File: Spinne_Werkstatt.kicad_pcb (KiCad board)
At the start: 2 copper layers, 42 x 82 mm, 17 parts, among them J1 Conn_01x02_Pin, J3 Conn_01x03_Pin, Q1 BSS138, Q2 BSS138, U1 ESP32-WROOM-32UE, U2 CH340C

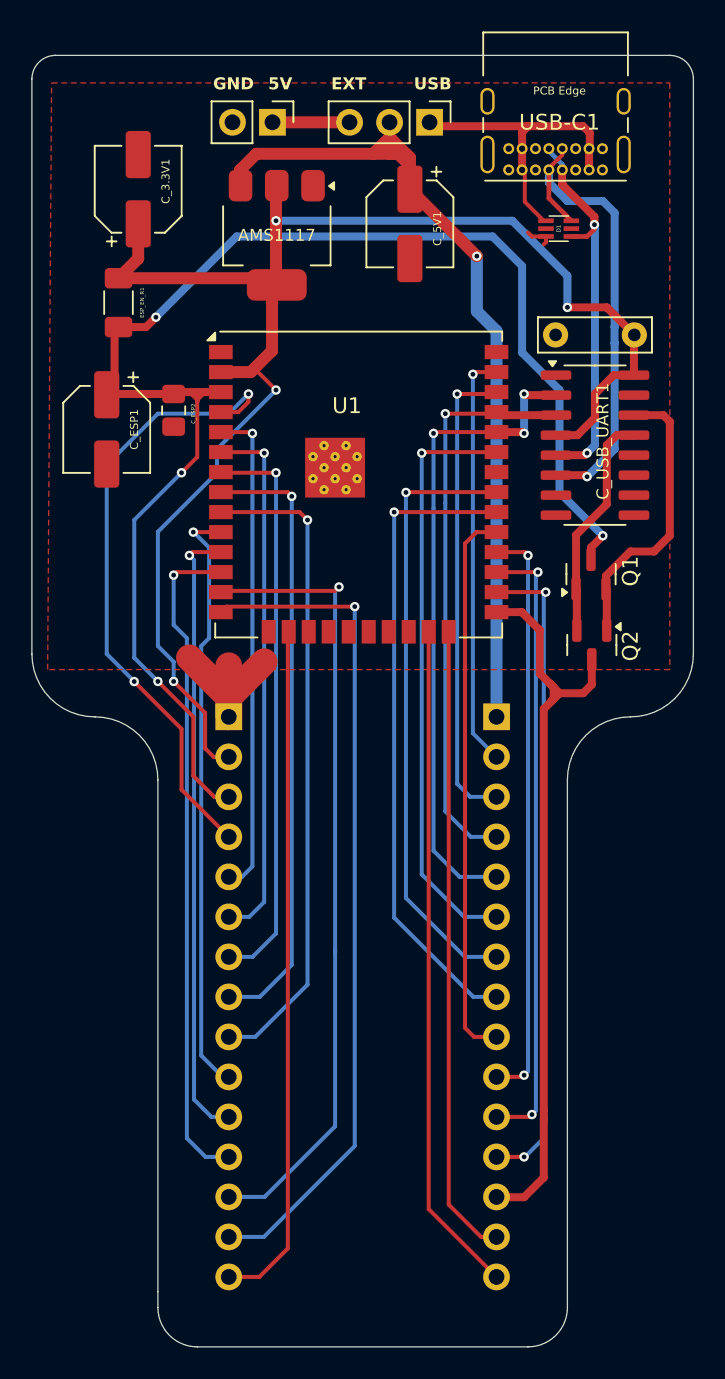
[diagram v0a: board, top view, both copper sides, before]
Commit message: improved ground plain -- version 1.1.2
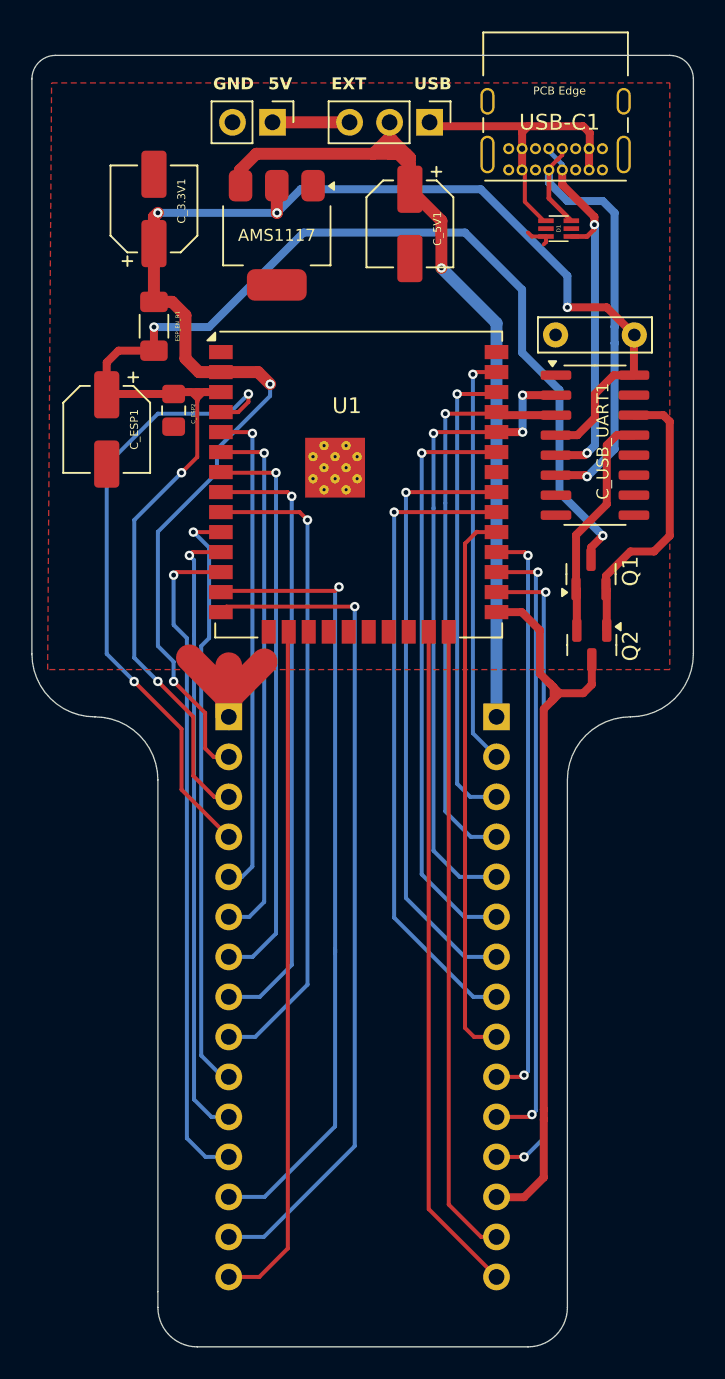
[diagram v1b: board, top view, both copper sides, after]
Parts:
- moved ESP_EN_R1 2.70 mm to (126.2, 52.7)
- moved C_3.3V1 1.60 mm to (126.2, 45.2)
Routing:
- net +3V3: track 96.1 -> 94.9 mm, vias 4 -> 5

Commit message: added IO Names, improved vias
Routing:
- net pin30: track 40.8 -> 43.2 mm
- net pin23: track 42.7 -> 44.2 mm
- net pin31: track 38.8 -> 40.2 mm
- net pin33: track 37.4 -> 38.8 mm
- net pin37: track 26.5 -> 27.8 mm
- net ESP_TX: track 36.3 -> 37.4 mm
- net ESP_RX: track 41.2 -> 42.2 mm
- net pin9: track 41.6 -> 42.6 mm
- net pin5: track 31.3 -> 32.2 mm
- net pin7: track 36.4 -> 37.1 mm
- net pin36: track 30.1 -> 30.9 mm
- net pin13: track 51.1 -> 50.4 mm
- net pin6: track 33.9 -> 34.6 mm
- net pin8: track 39.2 -> 39.8 mm
- net ESP32_EN: track 94.2 -> 93.5 mm
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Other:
- board text added: "3.3V"
- board text added: "EN"
- board text added: "GPIO12"
- board text added: "GPIO13"
- board text added: "GPIO14"
- board text added: "GPIO25"
- board text added: "GPIO26"
- board text added: "GPIO27"
- board text added: "GPIO32"
- board text added: "GPIO33"
- board text added: "GPIO34"
- board text added: "GPIO35"
- board text added: "VN"
- board text added: "VP"

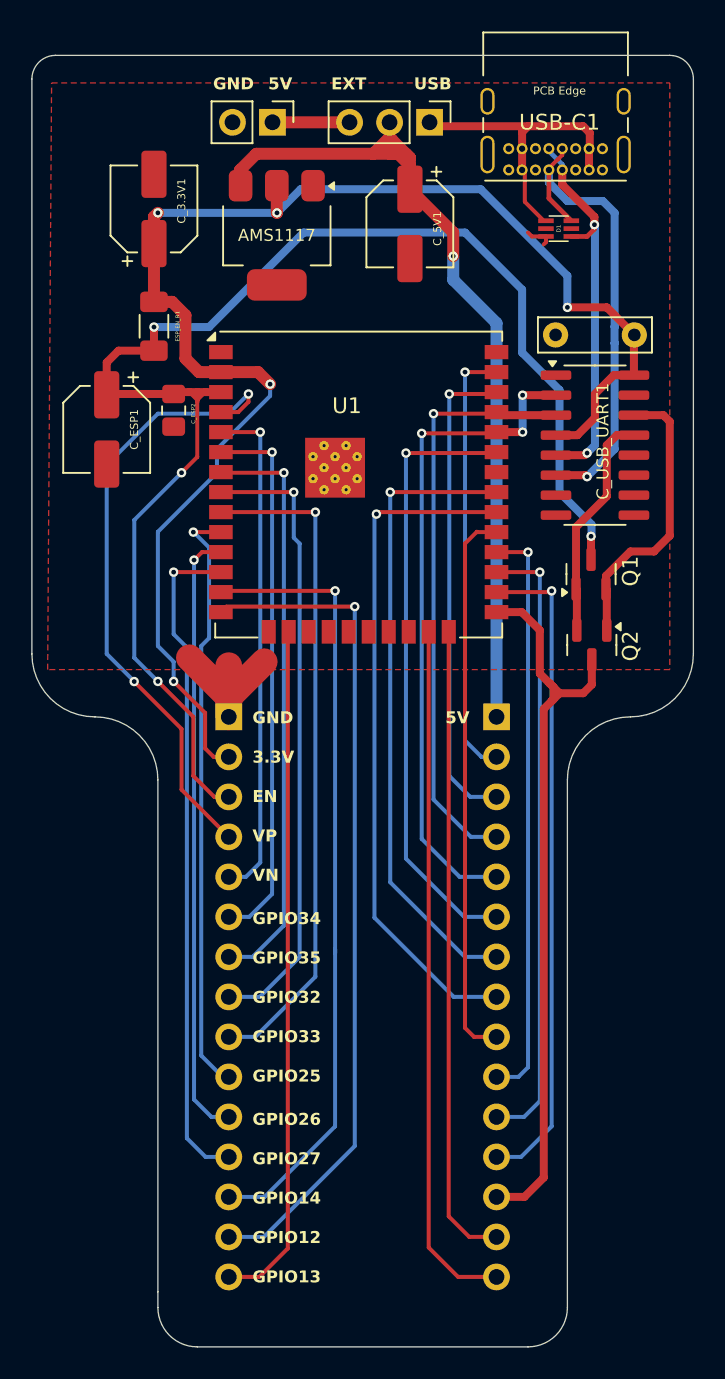
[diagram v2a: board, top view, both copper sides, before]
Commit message: improved clearences around uart capacitor
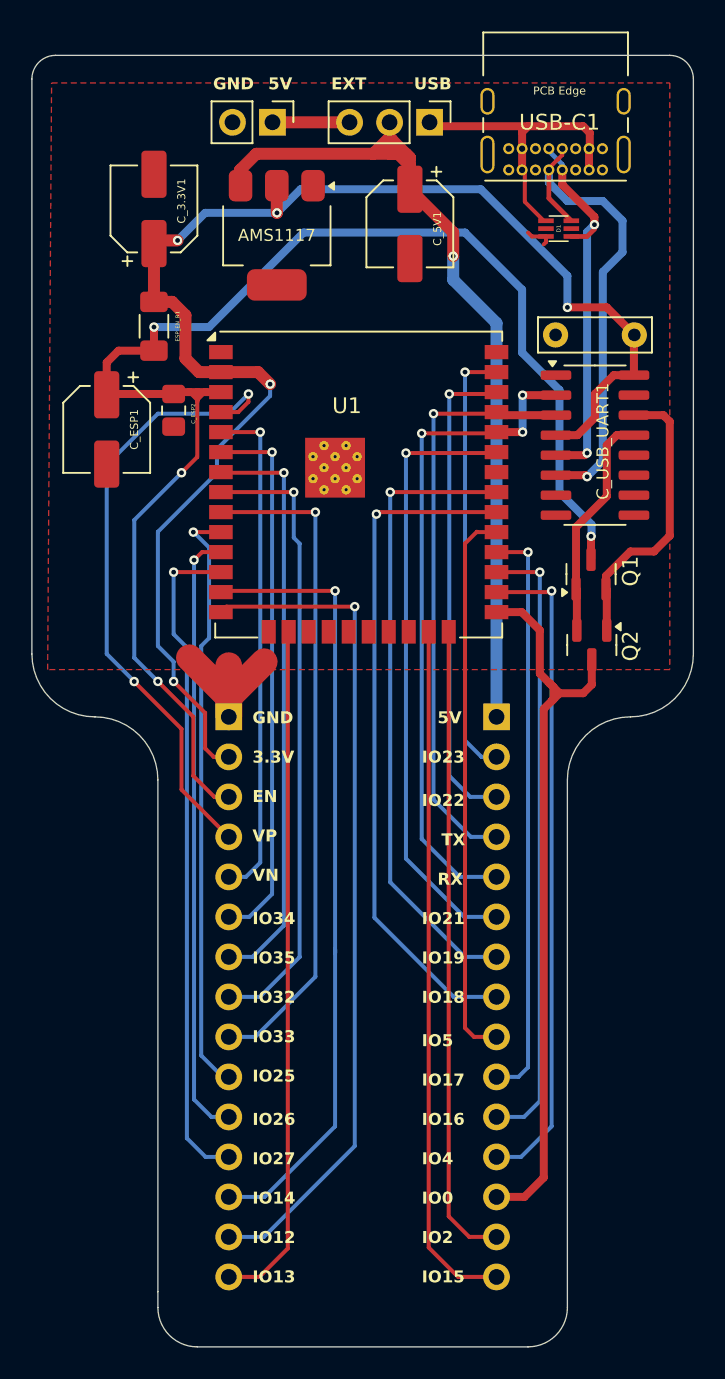
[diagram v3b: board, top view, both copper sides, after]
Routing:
- net +3V3: track 94.9 -> 93.9 mm
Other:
- board text added: "IO0"
- board text added: "IO12"
- board text added: "IO13"
- board text added: "IO14"
- board text added: "IO15"
- board text added: "IO16"
- board text added: "IO17"
- board text added: "IO18"
- board text added: "IO19"
- board text added: "IO2"
- board text added: "IO21"
- board text added: "IO22"
- board text added: "IO23"
- board text added: "IO25"
- board text added: "IO26"
- board text added: "IO27"
- board text added: "IO32"
- board text added: "IO33"
- board text added: "IO34"
- board text added: "IO35"
- board text added: "IO4"
- board text added: "IO5"
- board text added: "RX"
- board text added: "TX"
- board text removed: "GPIO12"
- board text removed: "GPIO13"
- board text removed: "GPIO14"
- board text removed: "GPIO25"
- board text removed: "GPIO26"
- board text removed: "GPIO27"
- board text removed: "GPIO32"
- board text removed: "GPIO33"
- board text removed: "GPIO34"
- board text removed: "GPIO35"
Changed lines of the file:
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@@
 		(layer "Edge.Cuts")
+	)
+	(gr_text "IO22"
+		(at 143.25 83.25 0)
+		(layer "F.SilkS")
+		(effects
+			(font
+				(size 0.762 0.762)
+				(thickness 0.1905)
+				(bold yes)
+			)
+			(justify left bottom)
+		)
 	)
 	(gr_text "USB"
@@
 	)
 	(gr_text "5V\n"
-		(at 144.75 78 0)
+		(at 144.25 78 0)
 		(layer "F.SilkS")
 		(effects
@@
 		)
 	)
-	(gr_text "GPIO25"
+	(gr_text "IO5"
+		(at 143.25 98.5 0)
+		(layer "F.SilkS")
+		(effects
+			(font
+				(size 0.762 0.762)
+				(thickness 0.1905)
+				(bold yes)
+			)
+			(justify left bottom)
+		)
+	)
+	(gr_text "IO25"
 		(at 132.5 100.75 0)
 		(layer "F.SilkS")
@@
 		)
 	)
-	(gr_text "GPIO26"
+	(gr_text "IO26"
 		(at 132.5 103.5 0)
 		(layer "F.SilkS")
@@
 		)
 	)
-	(gr_text "GPIO34"
+	(gr_text "IO34"
 		(at 132.5 90.75 0)
+		(layer "F.SilkS")
+		(effects
+			(font
+				(size 0.762 0.762)
+				(thickness 0.1905)
+				(bold yes)
+			)
+			(justify left bottom)
+		)
+	)
+	(gr_text "IO4"
+		(at 143.25 106 0)
 		(layer "F.SilkS")
 		(effects
@@
 		)
 	)
-	(gr_text "GPIO27\n"
+	(gr_text "TX\n"
+		(at 144.5 85.75 0)
+		(layer "F.SilkS")
+		(effects
+			(font
+				(size 0.762 0.762)
+				(thickness 0.1905)
+				(bold yes)
+			)
+			(justify left bottom)
+		)
+	)
+	(gr_text "IO23"
+		(at 143.25 80.5 0)
+		(layer "F.SilkS")
+		(effects
+			(font
+				(size 0.762 0.762)
+				(thickness 0.1905)
+				(bold yes)
+			)
+			(justify left bottom)
+		)
+	)
+	(gr_text "IO0"
+		(at 143.25 108.5 0)
+		(layer "F.SilkS")
+		(effects
+			(font
+				(size 0.762 0.762)
+				(thickness 0.1905)
+				(bold yes)
+			)
+			(justify left bottom)
+		)
+	)
+	(gr_text "IO2"
+		(at 143.25 111 0)
+		(layer "F.SilkS")
+		(effects
+			(font
+				(size 0.762 0.762)
+				(thickness 0.1905)
+				(bold yes)
+			)
+			(justify left bottom)
+		)
+	)
+	(gr_text "IO27\n"
 		(at 132.5 106 0)
 		(layer "F.SilkS")
@@
 		)
 	)
-	(gr_text "GPIO14"
+	(gr_text "IO15"
+		(at 143.25 113.5 0)
+		(layer "F.SilkS")
+		(effects
+			(font
+				(size 0.762 0.762)
+				(thickness 0.1905)
+				(bold yes)
+			)
+			(justify left bottom)
+		)
+	)
+	(gr_text "IO16"
+		(at 143.25 103.5 0)
+		(layer "F.SilkS")
+		(effects
+			(font
+				(size 0.762 0.762)
+				(thickness 0.1905)
+				(bold yes)
+			)
+			(justify left bottom)
+		)
+	)
+	(gr_text "IO21"
+		(at 143.25 90.75 0)
+		(layer "F.SilkS")
+		(effects
+			(font
+				(size 0.762 0.762)
+				(thickness 0.1905)
+				(bold yes)
+			)
+			(justify left bottom)
+		)
+	)
+	(gr_text "IO14"
 		(at 132.5 108.5 0)
 		(layer "F.SilkS")
@@
 		)
 	)
-	(gr_text "GPIO33"
+	(gr_text "IO18"
+		(at 143.25 95.75 0)
+		(layer "F.SilkS")
+		(effects
+			(font
+				(size 0.762 0.762)
+				(thickness 0.1905)
+				(bold yes)
+			)
+			(justify left bottom)
+		)
+	)
+	(gr_text "IO33"
 		(at 132.5 98.25 0)
 		(layer "F.SilkS")
@@
 		)
 	)
-	(gr_text "GPIO12"
+	(gr_text "IO12"
 		(at 132.5 111 0)
 		(layer "F.SilkS")
@@
 		)
 	)
-	(gr_text "GPIO13"
+	(gr_text "IO13"
 		(at 132.5 113.5 0)
 		(layer "F.SilkS")
@@
 		)
 	)
-	(gr_text "GPIO32"
+	(gr_text "RX"
+		(at 144.25 88.25 0)
+		(layer "F.SilkS")
+		(effects
+			(font
+				(size 0.762 0.762)
+				(thickness 0.1905)
+				(bold yes)
+			)
+			(justify left bottom)
+		)
+	)
+	(gr_text "IO32"
 		(at 132.5 95.75 0)
 		(layer "F.SilkS")
@@
 		)
 	)
-	(gr_text "GPIO35\n"
+	(gr_text "IO19"
+		(at 143.25 93.25 0)
+		(layer "F.SilkS")
+		(effects
+			(font
+				(size 0.762 0.762)
+				(thickness 0.1905)
+				(bold yes)
+			)
+			(justify left bottom)
+		)
+	)
+	(gr_text "IO17"
+		(at 143.25 101 0)
+		(layer "F.SilkS")
+		(effects
+			(font
+				(size 0.762 0.762)
+				(thickness 0.1905)
+				(bold yes)
+			)
+			(justify left bottom)
+		)
+	)
+	(gr_text "IO35\n"
 		(at 132.5 93.25 0)
 		(layer "F.SilkS")
@@
 	)
 	(segment
+		(start 126.45 47.25)
+		(end 126.25 47.45)
+		(width 0.762)
+		(layer "F.Cu")
+		(net 3)
+	)
+	(segment
 		(start 127.4 51.15)
 		(end 128.25 52)
@@
 	)
 	(segment
+		(start 127.75 47.25)
+		(end 126.45 47.25)
+		(width 0.762)
+		(layer "F.Cu")
+		(net 3)
+	)
+	(segment
 		(start 134.05 45.4888)
 		(end 134.0612 45.5)
@@
 	)
 	(segment
-		(start 126.5 45.5)
-		(end 126.25 45.75)
-		(width 0.762)
-		(layer "F.Cu")
-		(net 3)
-	)
-	(segment
 		(start 126.25 51.15)
 		(end 127.4 51.15)
@@
 	)
 	(segment
-		(start 126.25 45.75)
-		(end 126.25 47.45)
-		(width 0.762)
-		(layer "F.Cu")
-		(net 3)
-	)
-	(segment
 		(start 128.25 54.75)
 		(end 129.11 55.61)
@@
 	)
 	(via
-		(at 126.5 45.5)
+		(at 127.75 47.25)
 		(size 0.6)
 		(drill 0.3)
@@
 	)
 	(segment
+		(start 129.5 45.5)
+		(end 127.75 47.25)
+		(width 0.508)
+		(layer "B.Cu")
+		(net 3)
+	)
+	(segment
 		(start 152.5 49.5)
 		(end 152.5 51.5)
@@
 	(segment
 		(start 134.0612 45.5)
-		(end 126.5 45.5)
+		(end 129.5 45.5)
 		(width 0.508)
 		(layer "B.Cu")
@@
 	)
 	(segment
-		(start 154.25 46.283159)
-		(end 154.25 60.25)
+		(start 153.75 46.716841)
+		(end 153.75 60.75)
 		(width 0.508)
 		(layer "B.Cu")
@@
 	(segment
 		(start 154.216841 46.25)
-		(end 154.25 46.283159)
-		(width 0.508)
-		(layer "B.Cu")
-		(net 35)
-	)
-	(segment
-		(start 154.25 60.25)
-		(end 153.75 60.75)
+		(end 153.75 46.716841)
 		(width 0.508)
 		(layer "B.Cu")
@@
 	)
 	(segment
+		(start 156 48)
+		(end 156 46)
+		(width 0.508)
+		(layer "B.Cu")
+		(net 36)
+	)
+	(segment
+		(start 154.75 61.25)
+		(end 154.75 49.25)
+		(width 0.508)
+		(layer "B.Cu")
+		(net 36)
+	)
+	(segment
 		(start 152.5 44.75)
+		(end 151.325 43.575)
+		(width 0.508)
+		(layer "B.Cu")
+		(net 36)
+	)
+	(segment
+		(start 151.325 43.575)
+		(end 151.325 42.775)
+		(width 0.508)
+		(layer "B.Cu")
+		(net 36)
+	)
+	(segment
+		(start 154.75 44.75)
+		(end 152.5 44.75)
+		(width 0.508)
+		(layer "B.Cu")
+		(net 36)
+	)
+	(segment
+		(start 153.75 62.25)
+		(end 154.75 61.25)
+		(width 0.508)
+		(layer "B.Cu")
+		(net 36)
+	)
+	(segment
+		(start 154.75 49.25)
+		(end 156 48)
+		(width 0.508)
+		(layer "B.Cu")
+		(net 36)
+	)
+	(segment
+		(start 156 46)
 		(end 154.75 44.75)
 		(width 0.508)
 		(layer "B.Cu")
-		(net 36)
-	)
-	(segment
-		(start 155.495 53.769839)
-		(end 155.5 53.774839)
-		(width 0.508)
-		(layer "B.Cu")
-		(net 36)
-	)
-	(segment
-		(start 155.5 52.725161)
-		(end 155.495 52.730161)
-		(width 0.508)
-		(layer "B.Cu")
-		(net 36)
-	)
-	(segment
-		(start 155.5 53.774839)
-		(end 155.5 60.5)
-		(width 0.508)
-		(layer "B.Cu")
-		(net 36)
-	)
-	(segment
-		(start 151.325 42.775)
-		(end 151.325 43.575)
-		(width 0.508)
-		(layer "B.Cu")
-		(net 36)
-	)
-	(segment
-		(start 151.325 43.575)
-		(end 152.5 44.75)
-		(width 0.508)
-		(layer "B.Cu")
-		(net 36)
-	)
-	(segment
-		(start 154.75 44.75)
-		(end 155.5 45.5)
-		(width 0.508)
-		(layer "B.Cu")
-		(net 36)
-	)
-	(segment
-		(start 155.5 60.5)
-		(end 153.75 62.25)
-		(width 0.508)
-		(layer "B.Cu")
-		(net 36)
-	)
-	(segment
-		(start 155.5 45.5)
-		(end 155.5 52.725161)
-		(width 0.508)
-		(layer "B.Cu")
-		(net 36)
-	)
-	(segment
-		(start 155.495 52.730161)
-		(end 155.495 53.769839)
-		(width 0.508)
-		(layer "B.Cu")

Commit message: changed elko footprints, changed voltage regulator footprint
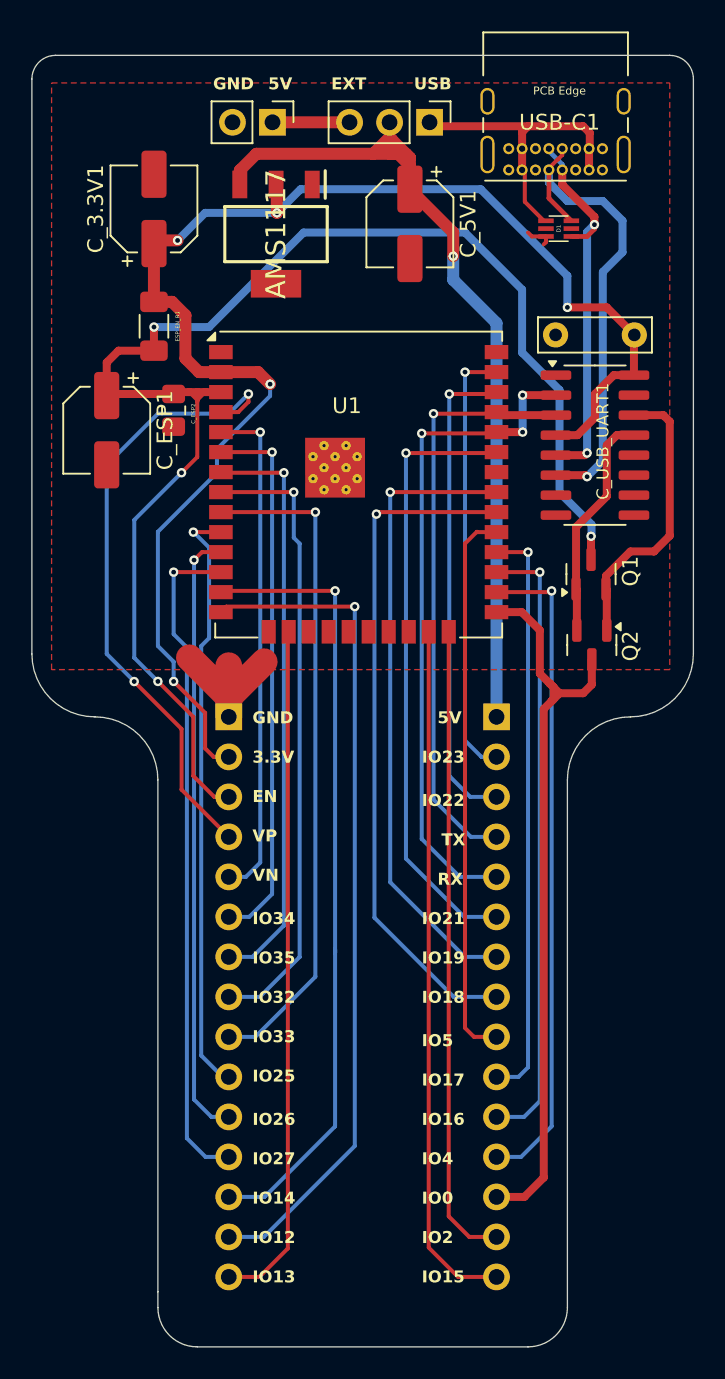
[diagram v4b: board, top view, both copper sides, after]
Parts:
- AMS1117: footprint Package_TO_SOT_SMD:SOT-223-3_TabPin2 -> bulme_footprints:SOT230P700X180-4N
- C_3.3V1, C_5V1, C_ESP1: footprint Capacitor_SMD:CP_Elec_5x5.7 -> Capacitor_SMD:CP_Elec_5x5.4
- moved AMS1117 0.09 mm to (134.0, 46.9)
